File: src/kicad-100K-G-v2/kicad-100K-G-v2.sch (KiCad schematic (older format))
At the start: 29 parts, among them P1 In, P2 Out, P3 Power, U1 TL072

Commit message: corrections 2014-09-01
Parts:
- C5: value 10n -> 6.8n
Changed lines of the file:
@@
 P 5550 4550
 F 0 "C5" V 5600 4650 40  0000 L CNN
-F 1 "10n" V 5450 4650 40  0000 L CNN
+F 1 "6.8n" V 5450 4650 40  0000 L CNN
 F 2 "Custom:C2-LARGE_PADS" H 5588 4400 30  0001 C CNN
 F 3 "" H 5550 4550 60  0000 C CNN

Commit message: 28/09/2014 minor changes
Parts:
- R10: value 500 -> 470
- R2: value 5Meg -> 4.7Meg
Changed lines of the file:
@@
 P 2450 4000
 F 0 "R2" V 2530 4000 40  0000 C CNN
-F 1 "5Meg" V 2457 4001 40  0000 C CNN
+F 1 "4.7Meg" V 2457 4001 40  0000 C CNN
 F 2 "Custom:R3-LARGE_PADS" V 2380 4000 30  0001 C CNN
 F 3 "" H 2450 4000 30  0000 C CNN
@@
 P 7450 5850
 F 0 "R10" V 7530 5850 40  0000 C CNN
-F 1 "500" V 7457 5851 40  0000 C CNN
+F 1 "470" V 7457 5851 40  0000 C CNN
 F 2 "Custom:R3-LARGE_PADS" V 7380 5850 30  0001 C CNN
 F 3 "" H 7450 5850 30  0000 C CNN

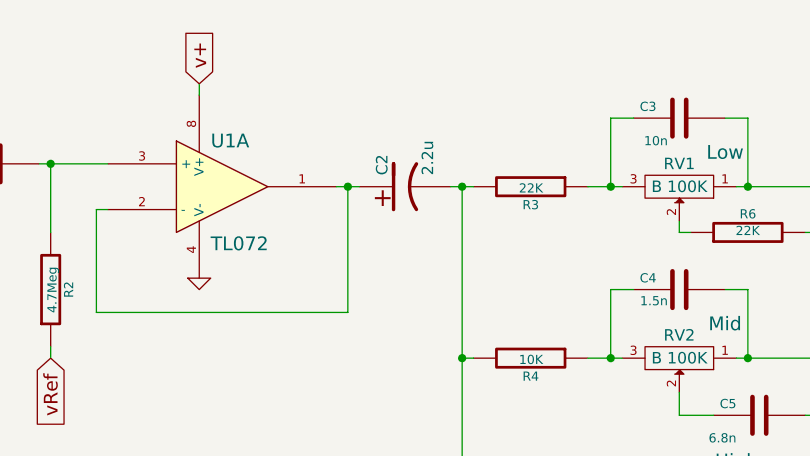
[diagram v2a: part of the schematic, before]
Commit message: 29/10/2014 corrections to 100K-G: version 2.1
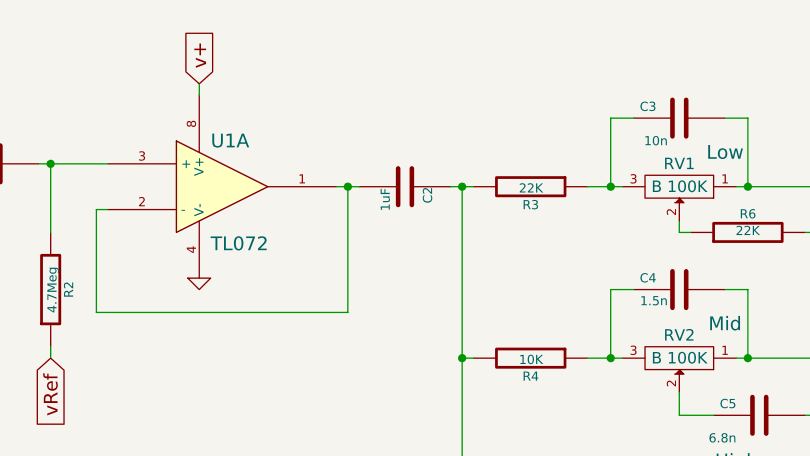
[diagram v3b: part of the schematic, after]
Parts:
- removed C2: 2.2u, Custom:C1.5V7-LARGE_PADS, symbol CP1
- added C2: 1uF, Custom:C2-LARGE_PADS, symbol C
- C7, C8, C9: footprint Custom:C1.5V7-LARGE_PADS -> Custom:C1V5-LARGE_PADS
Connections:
- net at U1.1, U1.2 (-): now also C2.2
- net at R3.2, R4.2, R5.2: now also C2.1
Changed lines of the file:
@@
 LIBS:power
 LIBS:kicad-100K-G-v2-cache
-EELAYER 24 0
+EELAYER 25 0
 EELAYER END
 $Descr A4 11693 8268
@@
 Sheet 1 1
 Title "Preamp 3EQ \"Lutherie Amateur\""
-Date "27 August 2014"
-Rev "V2"
+Date "29 October 2014"
+Rev "V2.1"
 Comp ""
 Comment1 "Guitar version, 100K pots"
@@
 F 0 "C7" H 8000 5950 50  0000 L CNN
 F 1 "10u" H 8000 5750 50  0000 L CNN
-F 2 "Custom:C1.5V7-LARGE_PADS" H 7950 5850 60  0001 C CNN
+F 2 "Custom:C1V5-LARGE_PADS" H 7950 5850 60  0001 C CNN
 F 3 "" H 7950 5850 60  0000 C CNN
 	1    7950 5850
@@
 F 0 "C8" H 9500 5000 50  0000 L CNN
 F 1 "1u" H 9500 4800 50  0000 L CNN
-F 2 "Custom:C1.5V7-LARGE_PADS" H 9450 4900 60  0001 C CNN
+F 2 "Custom:C1V5-LARGE_PADS" H 9450 4900 60  0001 C CNN
 F 3 "" H 9450 4900 60  0000 C CNN
 	1    9450 4900
@@
 F 0 "C9" H 9800 4650 50  0000 L CNN
 F 1 "10u" H 9800 4450 50  0000 L CNN
-F 2 "Custom:C1.5V7-LARGE_PADS" H 9750 4550 60  0001 C CNN
+F 2 "Custom:C1V5-LARGE_PADS" H 9750 4550 60  0001 C CNN
 F 3 "" H 9750 4550 60  0000 C CNN
 	1    9750 4550
@@
 +9V
 $Comp
-L CP1 C2
-U 1 1 53FE7685
-P 4000 3550
-F 0 "C2" H 4050 3650 50  0000 L CNN
-F 1 "2.2u" H 4050 3450 50  0000 L CNN
-F 2 "Custom:C1.5V7-LARGE_PADS" H 4000 3550 60  0001 C CNN
-F 3 "" H 4000 3550 60  0000 C CNN
-	1    4000 3550
-	0    -1   -1   0
-$EndComp
-$Comp
 L CONN_01X02 P2
 U 1 1 53FDE8A1
@@
 	5750 5150 6050 5150
 Connection ~ 5800 5150
+$Comp
+L C C2
+U 1 1 5450CF2F
+P 4000 3550
+F 0 "C2" H 4000 3650 40  0000 L CNN
+F 1 "1uF" H 4006 3465 40  0000 L CNN
+F 2 "Custom:C2-LARGE_PADS" H 4038 3400 30  0001 C CNN
+F 3 "" H 4000 3550 60  0000 C CNN
+	1    4000 3550
+	0    1    1    0
+$EndComp
 $EndSCHEMATC
